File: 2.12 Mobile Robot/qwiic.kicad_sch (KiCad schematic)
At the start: 18 parts, among them U2 TCA9548APWR

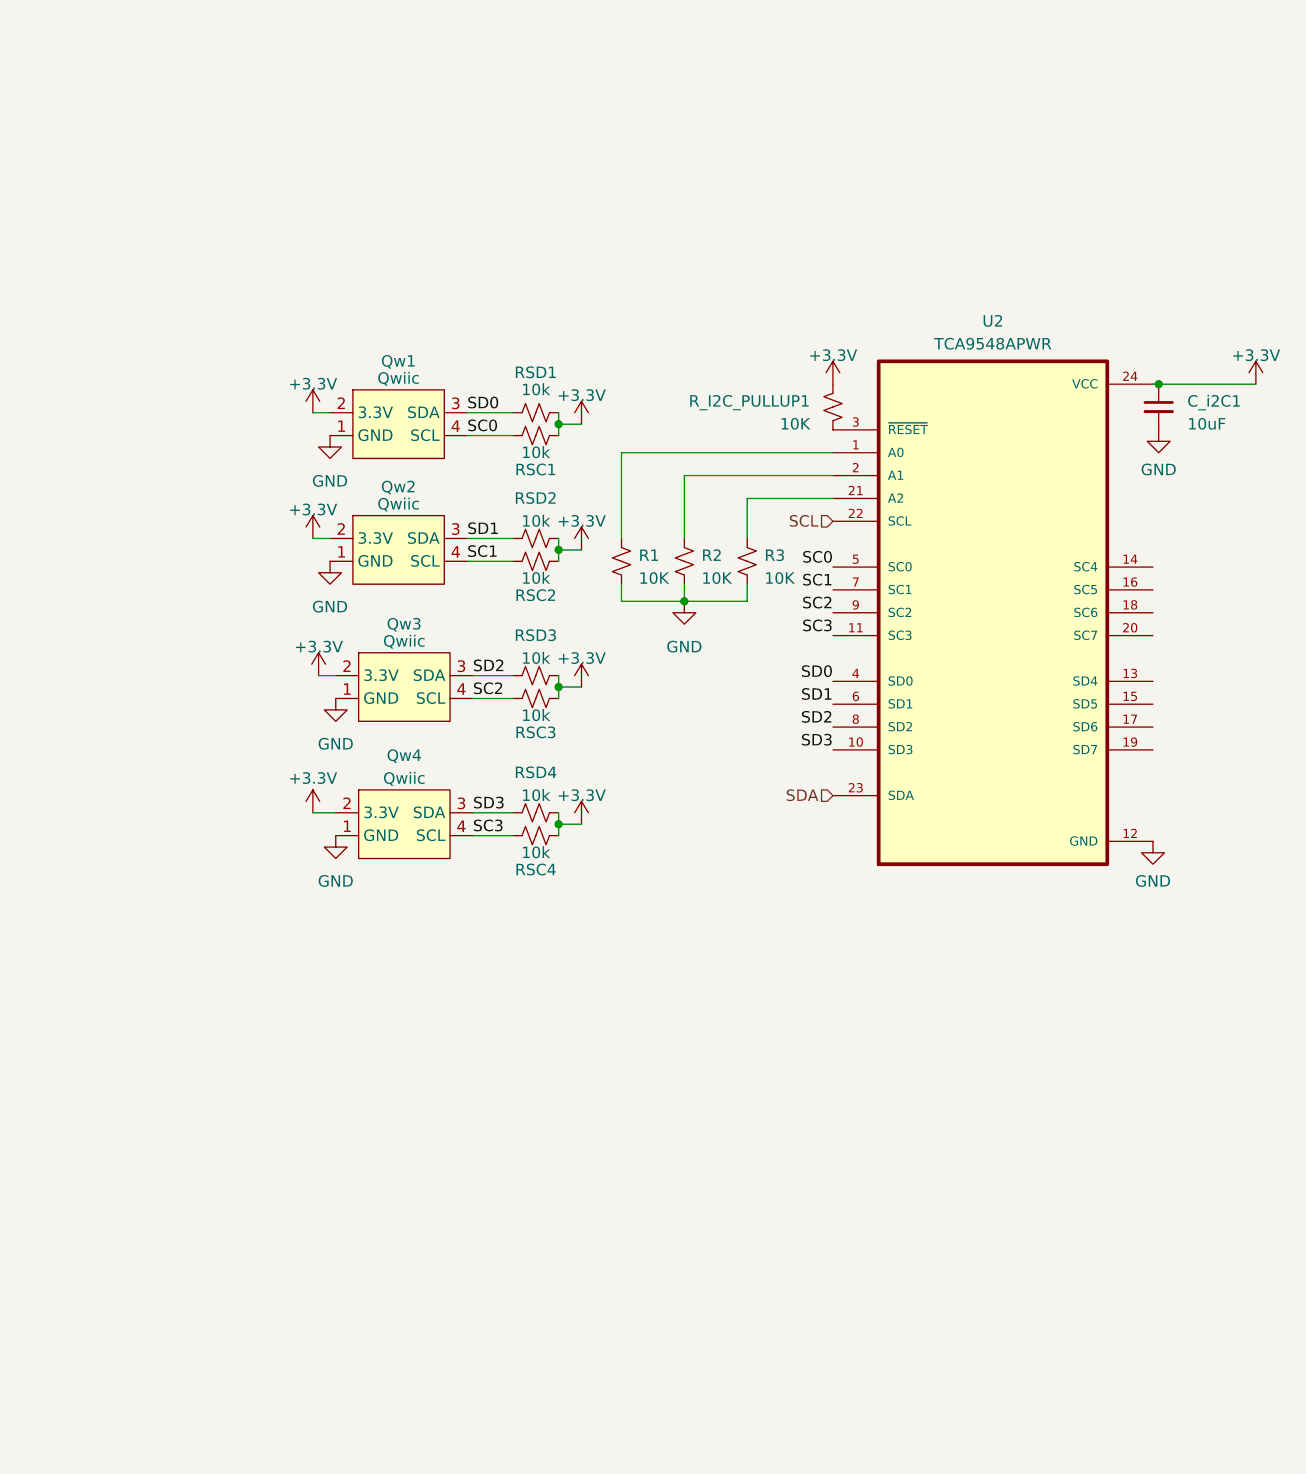
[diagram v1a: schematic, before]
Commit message: Changed some of the footprints
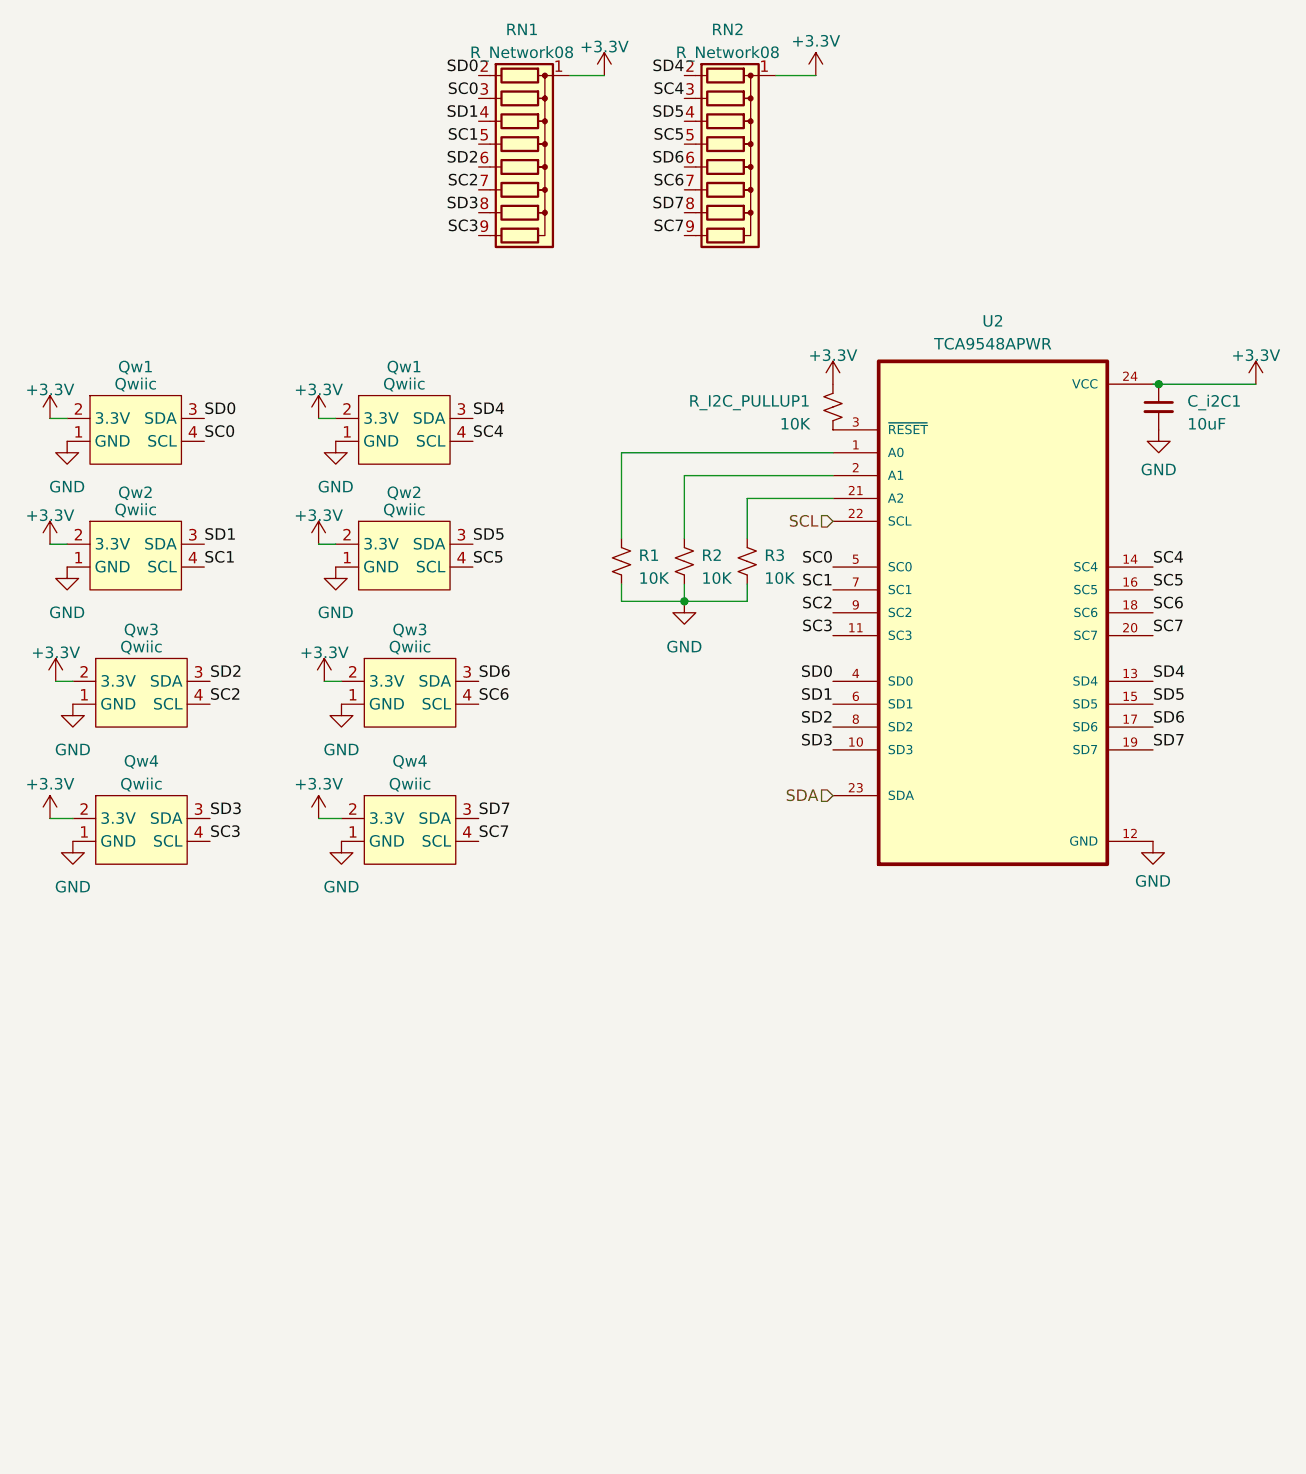
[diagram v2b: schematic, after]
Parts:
- removed RSC1, RSC2, RSC3, RSC4, RSD1, RSD2, RSD3, RSD4: 10k, Resistor_SMD:R_0402_1005Metric, symbol Device:R_Small_US
- added Qw1, Qw2, Qw3, Qw4: Qwiic, Connector_JST:JST_SH_BM04B-SRSS-TB_1x04-1MP_P1.00mm_Vertical, symbol Adafruit:Qwiic
- added RN1, RN2: R_Network08, Resistor_SMD:R_Array_Convex_5x1206, symbol Device:R_Network08
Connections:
- net +3.3V: now also Qw1.2 (3.3V), Qw2.2 (3.3V), Qw3.2 (3.3V), Qw4.2 (3.3V), RN1.1 (common), RN2.1 (common)
- net GND: now also Qw1.1 (GND), Qw2.1 (GND), Qw3.1 (GND), Qw4.1 (GND)
- net SC0: now also RN1.3 (R2)
- net SC1: now also RN1.5 (R4)
- net SC2: now also RN1.7 (R6)
- net SC3: now also RN1.9 (R8)
- net SD0: now also RN1.2 (R1)
- net SD1: now also RN1.4 (R3)
- net SD2: now also RN1.6 (R5)
- net SD3: now also RN1.8 (R7)
- net SD4: now reaches U2.13 (SD4)
- net SD4: now also Qw1.3 (SDA), RN2.2 (R1)
- net SC4: now reaches U2.14 (SC4)
- net SC4: now also Qw1.4 (SCL), RN2.3 (R2)
- net SD5: now reaches U2.15 (SD5)
- net SD5: now also Qw2.3 (SDA), RN2.4 (R3)
- net SC5: now reaches U2.16 (SC5)
- net SC5: now also Qw2.4 (SCL), RN2.5 (R4)
- net SD6: now reaches U2.17 (SD6)
- net SD6: now also Qw3.3 (SDA), RN2.6 (R5)
- net SC6: now reaches U2.18 (SC6)
- net SC6: now also Qw3.4 (SCL), RN2.7 (R6)
- net SD7: now reaches U2.19 (SD7)
- net SD7: now also Qw4.3 (SDA), RN2.8 (R7)
- net SC7: now reaches U2.20 (SC7)
- net SC7: now also Qw4.4 (SCL), RN2.9 (R8)
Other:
- moved on the sheet: Qw1, Qw2, Qw3, Qw4

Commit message: Renamed stuff
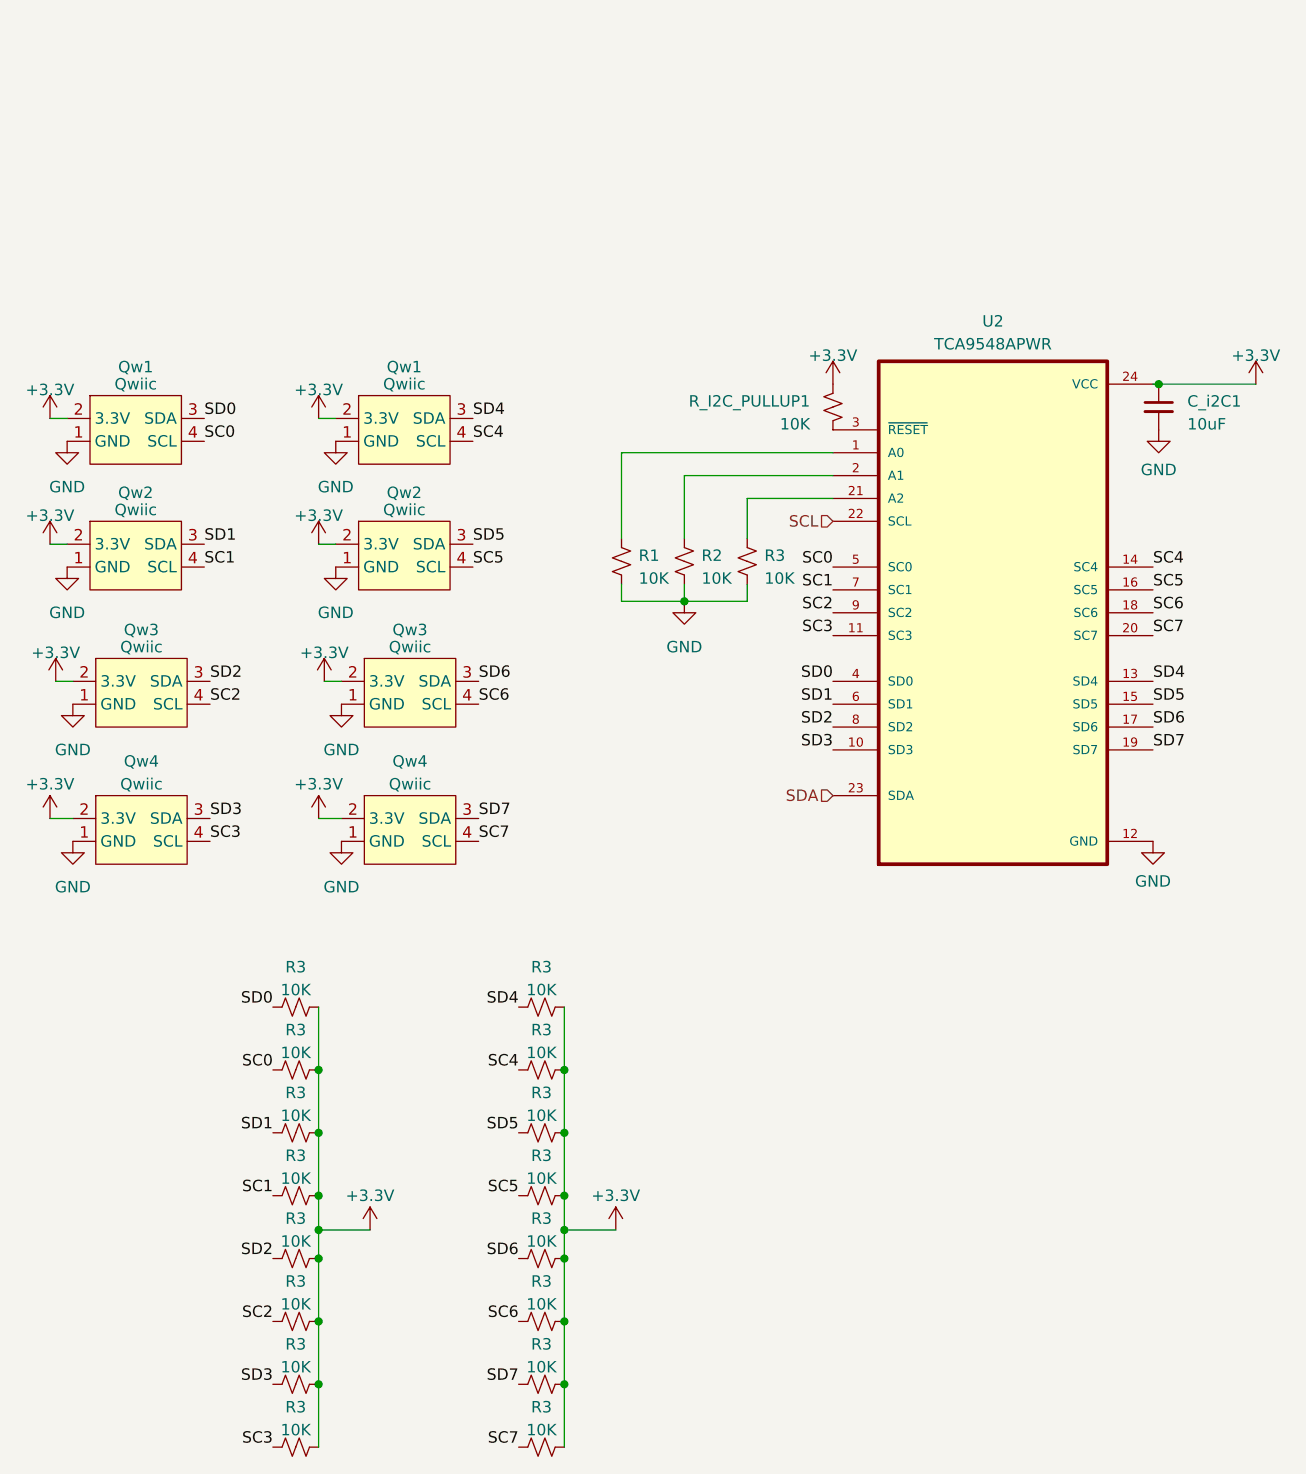
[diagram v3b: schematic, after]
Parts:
- removed RN1, RN2: R_Network08, Resistor_SMD:R_Array_Convex_5x1206, symbol Device:R_Network08
- added R3 (x16): 10K, Resistor_SMD:R_0201_0603Metric_Pad0.64x0.40mm_HandSolder, symbol Device:R_Small_US
- R1, R2, R3, R_I2C_PULLUP1: footprint Resistor_SMD:R_0402_1005Metric -> Resistor_SMD:R_0201_0603Metric_Pad0.64x0.40mm_HandSolder; MPN C144807 -> C22548
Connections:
- net +3.3V: now also R3.2, R3.2, R3.2, R3.2, R3.2, R3.2, R3.2, R3.2, R3.2, R3.2, R3.2, R3.2, R3.2, R3.2, R3.2, R3.2
- net SC0: now also R3.1
- net SC1: now also R3.1
- net SC2: now also R3.1
- net SC3: now also R3.1
- net SC4: now also R3.1
- net SC5: now also R3.1
- net SC6: now also R3.1
- net SC7: now also R3.1
- net SD0: now also R3.1
- net SD1: now also R3.1
- net SD2: now also R3.1
- net SD3: now also R3.1
- net SD4: now also R3.1
- net SD5: now also R3.1
- net SD6: now also R3.1
- net SD7: now also R3.1

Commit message: Made footprints from project libraries
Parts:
- U2: footprint 2.004:SOP65P640X120-24N -> 2.12_Mobile_Robot:SOP65P640X120-24N
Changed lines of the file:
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@@
       (effects (font (size 1.27 1.27)))
     )
-    (property "Footprint" "2.004:SOP65P640X120-24N" (at 146.05 80.01 0)
+    (property "Footprint" "2.12_Mobile_Robot:SOP65P640X120-24N" (at 146.05 80.01 0)
       (effects (font (size 1.27 1.27)) (justify bottom) hide)
     )

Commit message: Added silkscreen callouts and fixed resistors
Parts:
- R1, R2, R3, R_I2C_PULLUP1: footprint Resistor_SMD:R_0201_0603Metric_Pad0.64x0.40mm_HandSolder -> Resistor_SMD:R_0603_1608Metric
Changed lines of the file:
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@@
       (effects (font (size 1.27 1.27)))
     )
-    (property "Footprint" "Resistor_SMD:R_0201_0603Metric_Pad0.64x0.40mm_HandSolder" (at 95.885 137.795 0)
+    (property "Footprint" "Resistor_SMD:R_0603_1608Metric" (at 95.885 137.795 0)
       (effects (font (size 1.27 1.27)) hide)
     )
@@
       (effects (font (size 1.27 1.27)))
     )
-    (property "Footprint" "Resistor_SMD:R_0201_0603Metric_Pad0.64x0.40mm_HandSolder" (at 68.58 137.795 0)
+    (property "Footprint" "Resistor_SMD:R_0603_1608Metric" (at 68.58 137.795 0)
       (effects (font (size 1.27 1.27)) hide)
     )
@@
       (effects (font (size 1.27 1.27)) (justify left))
     )
-    (property "Footprint" "Resistor_SMD:R_0201_0603Metric_Pad0.64x0.40mm_HandSolder" (at 128.27 57.15 0)
+    (property "Footprint" "Resistor_SMD:R_0603_1608Metric" (at 128.27 57.15 0)
       (effects (font (size 1.27 1.27)) hide)
     )
@@
       (effects (font (size 1.27 1.27)))
     )
-    (property "Footprint" "Resistor_SMD:R_0201_0603Metric_Pad0.64x0.40mm_HandSolder" (at 68.58 165.735 0)
+    (property "Footprint" "Resistor_SMD:R_0603_1608Metric" (at 68.58 165.735 0)
       (effects (font (size 1.27 1.27)) hide)
     )
@@
       (effects (font (size 1.27 1.27)))
     )
-    (property "Footprint" "Resistor_SMD:R_0201_0603Metric_Pad0.64x0.40mm_HandSolder" (at 95.885 151.765 0)
+    (property "Footprint" "Resistor_SMD:R_0603_1608Metric" (at 95.885 151.765 0)
       (effects (font (size 1.27 1.27)) hide)
     )
@@
       (effects (font (size 1.27 1.27)))
     )
-    (property "Footprint" "Resistor_SMD:R_0201_0603Metric_Pad0.64x0.40mm_HandSolder" (at 68.58 123.825 0)
+    (property "Footprint" "Resistor_SMD:R_0603_1608Metric" (at 68.58 123.825 0)
       (effects (font (size 1.27 1.27)) hide)
     )
@@
       (effects (font (size 1.27 1.27)))
     )
-    (property "Footprint" "Resistor_SMD:R_0201_0603Metric_Pad0.64x0.40mm_HandSolder" (at 95.885 165.735 0)
+    (property "Footprint" "Resistor_SMD:R_0603_1608Metric" (at 95.885 165.735 0)
       (effects (font (size 1.27 1.27)) hide)
     )
@@
       (effects (font (size 1.27 1.27)))
     )
-    (property "Footprint" "Resistor_SMD:R_0201_0603Metric_Pad0.64x0.40mm_HandSolder" (at 95.885 130.81 0)
+    (property "Footprint" "Resistor_SMD:R_0603_1608Metric" (at 95.885 130.81 0)
       (effects (font (size 1.27 1.27)) hide)
     )
@@
       (effects (font (size 1.27 1.27)) (justify left))
     )
-    (property "Footprint" "Resistor_SMD:R_0201_0603Metric_Pad0.64x0.40mm_HandSolder" (at 104.775 74.295 0)
+    (property "Footprint" "Resistor_SMD:R_0603_1608Metric" (at 104.775 74.295 0)
       (effects (font (size 1.27 1.27)) hide)
     )
@@
       (effects (font (size 1.27 1.27)))
     )
-    (property "Footprint" "Resistor_SMD:R_0201_0603Metric_Pad0.64x0.40mm_HandSolder" (at 68.58 172.72 0)
+    (property "Footprint" "Resistor_SMD:R_0603_1608Metric" (at 68.58 172.72 0)
       (effects (font (size 1.27 1.27)) hide)
     )
@@
       (effects (font (size 1.27 1.27)) (justify left))
     )
-    (property "Footprint" "Resistor_SMD:R_0201_0603Metric_Pad0.64x0.40mm_HandSolder" (at 111.76 74.295 0)
+    (property "Footprint" "Resistor_SMD:R_0603_1608Metric" (at 111.76 74.295 0)
       (effects (font (size 1.27 1.27)) hide)
     )
@@
       (effects (font (size 1.27 1.27)) (justify left))
     )
-    (property "Footprint" "Resistor_SMD:R_0201_0603Metric_Pad0.64x0.40mm_HandSolder" (at 118.745 74.295 0)
+    (property "Footprint" "Resistor_SMD:R_0603_1608Metric" (at 118.745 74.295 0)
       (effects (font (size 1.27 1.27)) hide)
     )
@@
       (effects (font (size 1.27 1.27)))
     )
-    (property "Footprint" "Resistor_SMD:R_0201_0603Metric_Pad0.64x0.40mm_HandSolder" (at 68.58 144.78 0)
+    (property "Footprint" "Resistor_SMD:R_0603_1608Metric" (at 68.58 144.78 0)
       (effects (font (size 1.27 1.27)) hide)
     )
@@
       (effects (font (size 1.27 1.27)))
     )
-    (property "Footprint" "Resistor_SMD:R_0201_0603Metric_Pad0.64x0.40mm_HandSolder" (at 95.885 144.78 0)
+    (property "Footprint" "Resistor_SMD:R_0603_1608Metric" (at 95.885 144.78 0)
       (effects (font (size 1.27 1.27)) hide)
     )
@@
       (effects (font (size 1.27 1.27)))
     )
-    (property "Footprint" "Resistor_SMD:R_0201_0603Metric_Pad0.64x0.40mm_HandSolder" (at 68.58 151.765 0)
+    (property "Footprint" "Resistor_SMD:R_0603_1608Metric" (at 68.58 151.765 0)
       (effects (font (size 1.27 1.27)) hide)
     )
@@
       (effects (font (size 1.27 1.27)))
     )
-    (property "Footprint" "Resistor_SMD:R_0201_0603Metric_Pad0.64x0.40mm_HandSolder" (at 68.58 158.75 0)
+    (property "Footprint" "Resistor_SMD:R_0603_1608Metric" (at 68.58 158.75 0)
       (effects (font (size 1.27 1.27)) hide)
     )
@@
       (effects (font (size 1.27 1.27)))
     )
-    (property "Footprint" "Resistor_SMD:R_0201_0603Metric_Pad0.64x0.40mm_HandSolder" (at 95.885 158.75 0)
+    (property "Footprint" "Resistor_SMD:R_0603_1608Metric" (at 95.885 158.75 0)
       (effects (font (size 1.27 1.27)) hide)
     )
@@
       (effects (font (size 1.27 1.27)))
     )
-    (property "Footprint" "Resistor_SMD:R_0201_0603Metric_Pad0.64x0.40mm_HandSolder" (at 95.885 172.72 0)
+    (property "Footprint" "Resistor_SMD:R_0603_1608Metric" (at 95.885 172.72 0)
       (effects (font (size 1.27 1.27)) hide)
     )
@@
       (effects (font (size 1.27 1.27)))
     )
-    (property "Footprint" "Resistor_SMD:R_0201_0603Metric_Pad0.64x0.40mm_HandSolder" (at 68.58 130.81 0)
+    (property "Footprint" "Resistor_SMD:R_0603_1608Metric" (at 68.58 130.81 0)
       (effects (font (size 1.27 1.27)) hide)
     )
@@
   )
   (symbol (lib_id "Device:R_Small_US") (at 95.885 123.825 90) (unit 1)
-    (in_bom yes) (on_board yes) (dnp no) (fields_autoplaced)
+    (in_bom yes) (on_board yes) (dnp no)
     (property "Reference" "R3" (at 95.885 119.38 90)
       (effects (font (size 1.27 1.27)))
@@
       (effects (font (size 1.27 1.27)))
     )
-    (property "Footprint" "Resistor_SMD:R_0201_0603Metric_Pad0.64x0.40mm_HandSolder" (at 95.885 123.825 0)
-      (effects (font (size 1.27 1.27)) hide)
-    )
+    (property "Footprint" "Resistor_SMD:R_0603_1608Metric" (at 95.885 123.825 0)
+      (effects (font (size 1.27 1.27)) hide)
+    )

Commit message: Tentatively ready for production
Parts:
- C_i2C1: footprint Capacitor_SMD:C_0805_2012Metric_Pad1.18x1.45mm_HandSolder -> footprint:0805_2012Metric; symbol Device:C_Small -> jlcpcb-basic-capacitor:0805,10uF,25V,X5R; LCSC (none) -> C15850; MFG (none) -> Samsung Electro-Mechanics; MFGPN (none) -> CL21A106KAYNNNE
- R1, R2, R3, R_I2C_PULLUP1: footprint Resistor_SMD:R_0603_1608Metric -> footprint:0603_1608Metric; symbol Device:R_Small_US -> jlcpcb-basic-resistor:0603,10k; LCSC (none) -> C25804; MFG (none) -> UNI-ROYAL(Uniroyal Elec); MFGPN (none) -> 0603WAF1002T5E
- U2: symbol TCA9548APWR:TCA9548APWR -> 2.12 Symbols:TCA9548APWR
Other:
- company: (none) -> MIT - jntaimo
- title: (none) -> I2C Multiplexer

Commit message: Updated to Kicad 8
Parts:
- renumbered C_i2C1 to C1, Qw1 to Qw5, Qw2 to Qw6, Qw3 to Qw7, Qw4 to Qw8, R3 to R10, R3 to R11, R3 to R12, R3 to R13, R3 to R14, R3 to R15, R3 to R16, R3 to R17, R3 to R18, R3 to R19, R3 to R20, R3 to R21, R1 to R22, R2 to R23, R3 to R24, R_I2C_PULLUP1 to R25, R3 to R6, R3 to R7, R3 to R8, R3 to R9, U2 to U3
